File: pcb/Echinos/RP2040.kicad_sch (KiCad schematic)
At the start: 19 parts, among them U2 RP2040, X1 ASE-12MHz

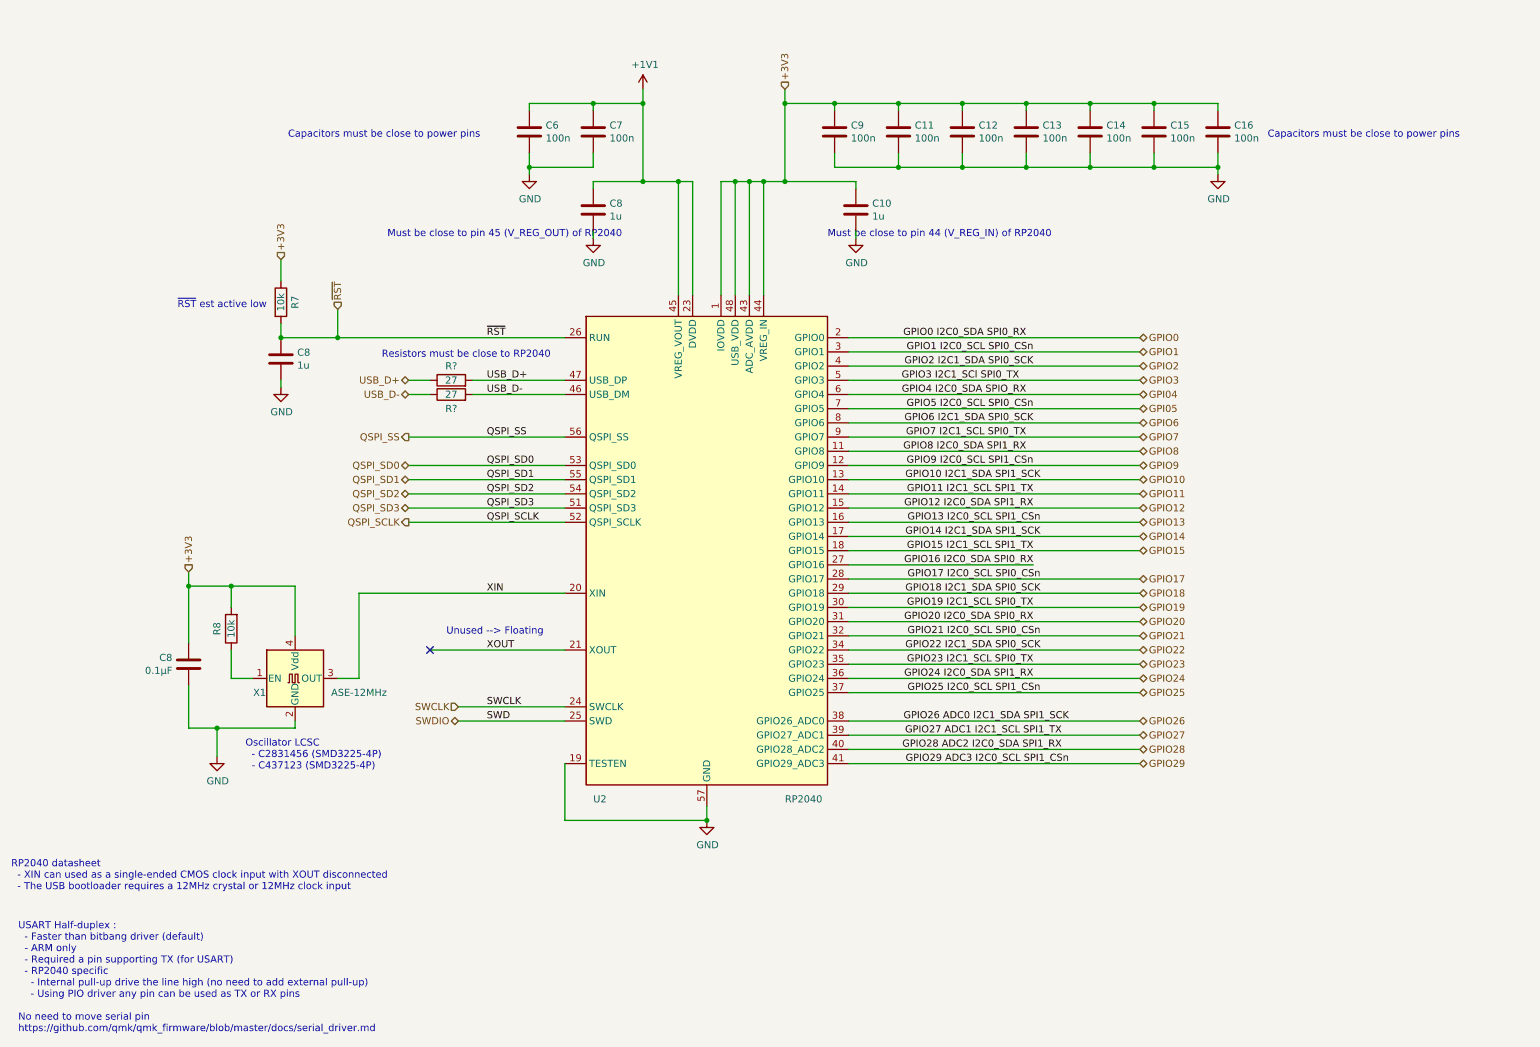
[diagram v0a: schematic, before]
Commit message: ✨ ♻️ 🚧 [PCB] - Continue draft schematic with:   - Keyboard matrix + Rotary encoder + analog joystick (specific sheet)   - Rename RP2040 sheet from untitled to RP2040 (make more sense ...)   - MCU first pin assignation
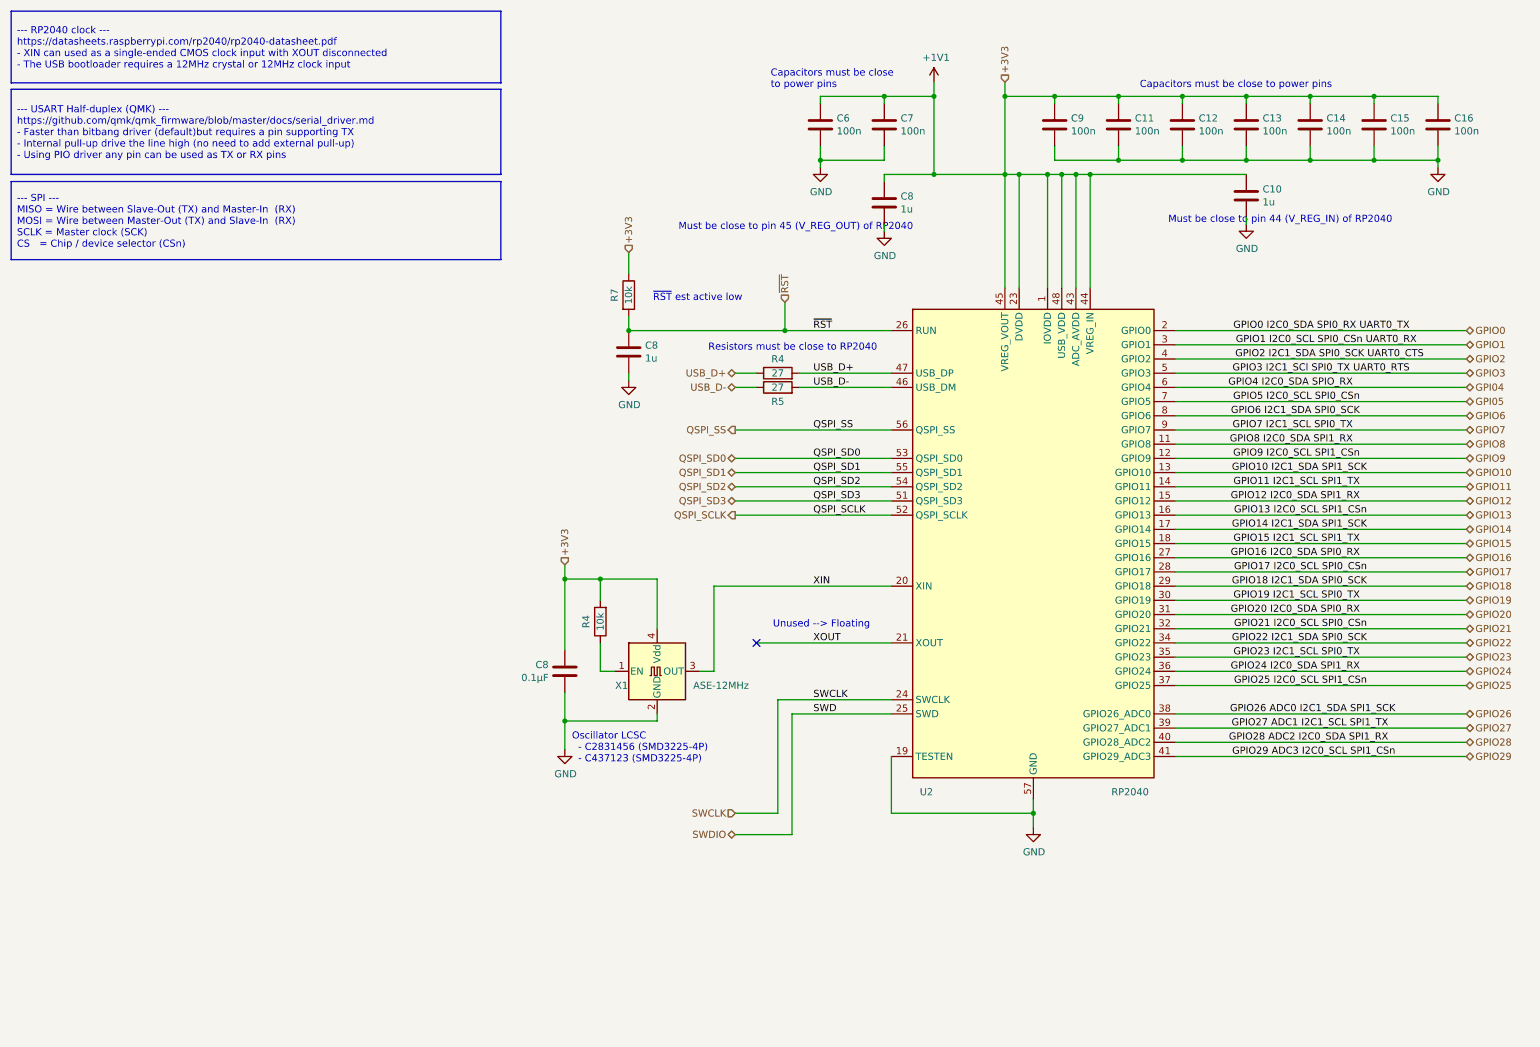
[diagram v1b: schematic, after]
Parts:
- gave numbers to parts that had none: 2
- renumbered R8 to R4
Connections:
- net +3V3 is gone; now on net +1V1: C10.1, C11.1, C12.1, C13.1, C14.1, C15.1, C16.1, C8.1, C9.1, R4.2, R7.1, U2.1 (IOVDD), U2.10 (IOVDD), U2.22 (IOVDD), U2.33 (IOVDD), U2.42 (IOVDD), U2.43 (ADC_AVDD), U2.44 (VREG_IN), U2.48 (USB_VDD), U2.49 (IOVDD), X1.4 (Vdd)
- net GPIO16 I2C0_SDA SPI0_RX renamed GPIO16
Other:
- note removed: "RP2040 datasheet - XIN can used as a single-ended CMOS clock input with XOUT disconnected - The USB bootloader requires a 12MHz crystal or 12MHz clock input"
- note removed: "USART Half-duplex : - Faster than bitbang driver (default) - ARM only - Required a pin supporting TX (for USART) - RP2040 specific - Internal pull-up drive the line high (no need to add external pull-up) - Using PIO driver any pin can be used as TX or RX pins No need to move serial pin https://github.com/qmk/qmk_firmware/blob/master/docs/serial_driver.md"
- moved on the sheet: C10, C11, C12, C13, C14, C15, C16, C6, C7, C8, C9, R4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

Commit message: ♻️ [PCB] - Remove symbol instances linking to other projets due to copy and paste of component symbol.
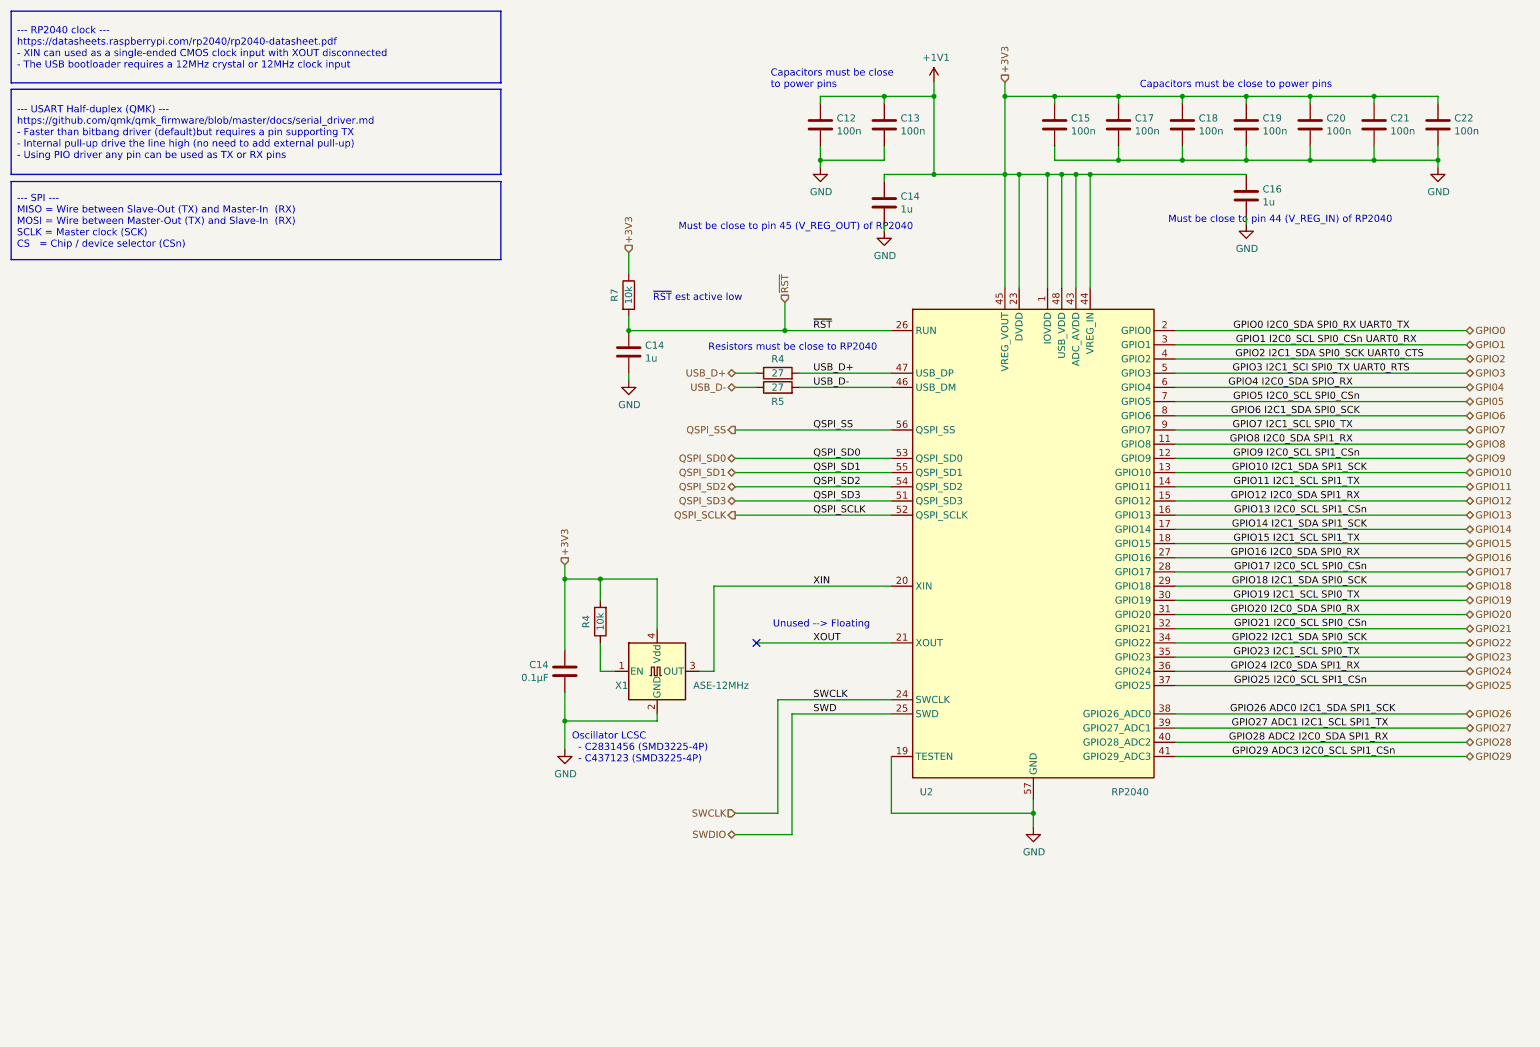
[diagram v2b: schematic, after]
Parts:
- renumbered C6 to C12, C7 to C13, C8 to C14, C9 to C15, C10 to C16, C11 to C17, C12 to C18, C13 to C19, C14 to C20, C15 to C21, C16 to C22

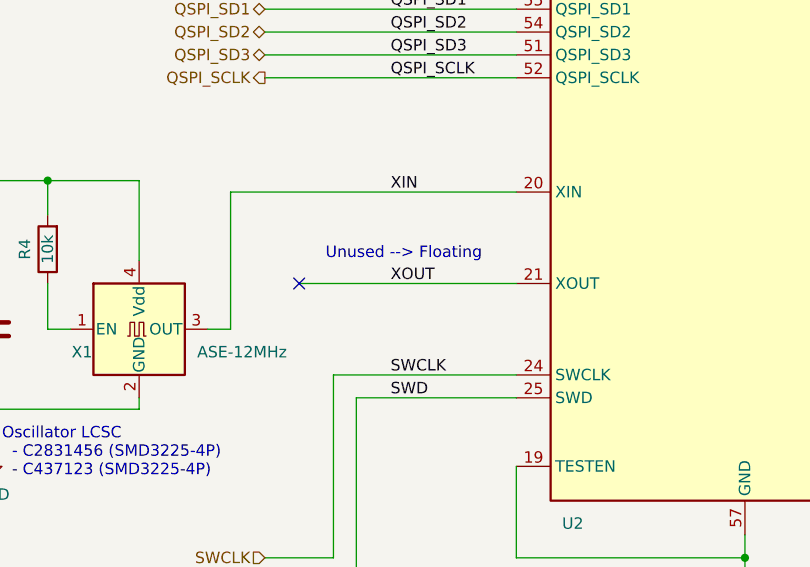
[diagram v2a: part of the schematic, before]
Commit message: ♻️ [PCB] - Add ferrite bead between shield and ground. Assign hand solder footprints whenever possible. Complete footprint assignation.
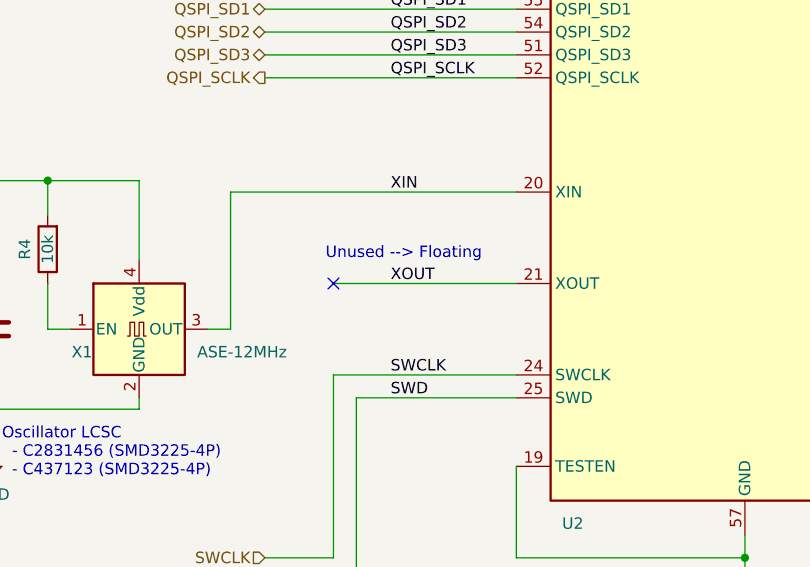
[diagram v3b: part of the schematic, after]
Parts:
- C12, C13, C14, C15, C16, C17, C18, C19, C20, C21, C22: footprint Capacitor_SMD:C_0402_1005Metric -> Capacitor_SMD:C_0402_1005Metric_Pad0.74x0.62mm_HandSolder
- R4, R5, R7: footprint Resistor_SMD:R_0402_1005Metric -> Resistor_SMD:R_0402_1005Metric_Pad0.72x0.64mm_HandSolder
- U2: footprint Package_DFN_QFN:QFN-56-1EP_7x7mm_P0.4mm_EP3.2x3.2mm -> Echinos:RP2040-QFN-56
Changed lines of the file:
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@@
   (junction (at 257.81 27.94) (diameter 0) (color 0 0 0 0)
   )
-  (no_connect (at 147.32 125.73))
+  (no_connect (at 151.13 125.73))
   (wire (pts (xy 204.47 41.91) (xy 201.93 41.91))
     (stroke (width 0) (type default))
@@
     (stroke (width 0) (type default))
   )
-  (wire (pts (xy 147.32 125.73) (xy 171.45 125.73))
+  (wire (pts (xy 151.13 125.73) (xy 171.45 125.73))
     (stroke (width 0) (type default))
   )
@@
       (effects (font (size 1.27 1.27)) (justify left))
     )
-    (property "Footprint" "Capacitor_SMD:C_0402_1005Metric" (at 235.9152 49.53 0)
+    (property "Footprint" "Capacitor_SMD:C_0402_1005Metric_Pad0.74x0.62mm_HandSolder" (at 235.9152 49.53 0)
       (effects (font (size 1.27 1.27)) hide)
     )
@@
       (effects (font (size 1.27 1.27)))
     )
-    (property "Footprint" "Resistor_SMD:R_0402_1005Metric" (at 122.682 63.5 90)
+    (property "Footprint" "Resistor_SMD:R_0402_1005Metric_Pad0.72x0.64mm_HandSolder" (at 122.682 63.5 90)
       (effects (font (size 1.27 1.27)) hide)
     )
@@
       (effects (font (size 1.27 1.27)) (justify left))
     )
-    (property "Footprint" "Capacitor_SMD:C_0402_1005Metric" (at 112.0648 134.62 0)
+    (property "Footprint" "Capacitor_SMD:C_0402_1005Metric_Pad0.74x0.62mm_HandSolder" (at 112.0648 134.62 0)
       (effects (font (size 1.27 1.27)) hide)
     )
@@
       (effects (font (size 1.27 1.27)) (justify left))
     )
-    (property "Footprint" "Capacitor_SMD:C_0402_1005Metric" (at 224.4852 36.83 0)
+    (property "Footprint" "Capacitor_SMD:C_0402_1005Metric_Pad0.74x0.62mm_HandSolder" (at 224.4852 36.83 0)
       (effects (font (size 1.27 1.27)) hide)
     )
@@
       (effects (font (size 1.27 1.27)) (justify left))
     )
-    (property "Footprint" "Capacitor_SMD:C_0402_1005Metric" (at 213.0552 36.83 0)
+    (property "Footprint" "Capacitor_SMD:C_0402_1005Metric_Pad0.74x0.62mm_HandSolder" (at 213.0552 36.83 0)
       (effects (font (size 1.27 1.27)) hide)
     )
@@
       (effects (font (size 1.27 1.27)) (justify left))
     )
-    (property "Footprint" "Capacitor_SMD:C_0402_1005Metric" (at 125.4252 77.47 0)
+    (property "Footprint" "Capacitor_SMD:C_0402_1005Metric_Pad0.74x0.62mm_HandSolder" (at 125.4252 77.47 0)
       (effects (font (size 1.27 1.27)) hide)
     )
@@
       (effects (font (size 1.27 1.27)) (justify left))
     )
-    (property "Footprint" "Capacitor_SMD:C_0402_1005Metric" (at 171.1452 36.83 0)
+    (property "Footprint" "Capacitor_SMD:C_0402_1005Metric_Pad0.74x0.62mm_HandSolder" (at 171.1452 36.83 0)
       (effects (font (size 1.27 1.27)) hide)
     )
@@
       (effects (font (size 1.27 1.27)) (justify left))
     )
-    (property "Footprint" "Capacitor_SMD:C_0402_1005Metric" (at 247.3452 36.83 0)
+    (property "Footprint" "Capacitor_SMD:C_0402_1005Metric_Pad0.74x0.62mm_HandSolder" (at 247.3452 36.83 0)
       (effects (font (size 1.27 1.27)) hide)
     )
@@
       (effects (font (size 1.27 1.27)) (justify left))
     )
-    (property "Footprint" "Capacitor_SMD:C_0402_1005Metric" (at 159.7152 36.83 0)
+    (property "Footprint" "Capacitor_SMD:C_0402_1005Metric_Pad0.74x0.62mm_HandSolder" (at 159.7152 36.83 0)
       (effects (font (size 1.27 1.27)) hide)
     )
@@
       (effects (font (size 1.27 1.27)) (justify left))
     )
-    (property "Footprint" "Capacitor_SMD:C_0402_1005Metric" (at 235.9152 36.83 0)
+    (property "Footprint" "Capacitor_SMD:C_0402_1005Metric_Pad0.74x0.62mm_HandSolder" (at 235.9152 36.83 0)
       (effects (font (size 1.27 1.27)) hide)
     )
@@
       (effects (font (size 1.27 1.27)) (justify left))
     )
-    (property "Footprint" "Capacitor_SMD:C_0402_1005Metric" (at 270.2052 36.83 0)
+    (property "Footprint" "Capacitor_SMD:C_0402_1005Metric_Pad0.74x0.62mm_HandSolder" (at 270.2052 36.83 0)
       (effects (font (size 1.27 1.27)) hide)
     )
@@
       (effects (font (size 1.27 1.27)))
     )
-    (property "Footprint" "Resistor_SMD:R_0402_1005Metric" (at 151.13 81.788 90)
+    (property "Footprint" "Resistor_SMD:R_0402_1005Metric_Pad0.72x0.64mm_HandSolder" (at 151.13 81.788 90)
       (effects (font (size 1.27 1.27)) hide)
     )
@@
       (effects (font (size 1.27 1.27)) (justify left))
     )
-    (property "Footprint" "Capacitor_SMD:C_0402_1005Metric" (at 171.1452 50.8 0)
+    (property "Footprint" "Capacitor_SMD:C_0402_1005Metric_Pad0.74x0.62mm_HandSolder" (at 171.1452 50.8 0)
       (effects (font (size 1.27 1.27)) hide)
     )
@@
       (effects (font (size 1.27 1.27)))
     )
-    (property "Footprint" "Resistor_SMD:R_0402_1005Metric" (at 121.158 121.92 90)
+    (property "Footprint" "Resistor_SMD:R_0402_1005Metric_Pad0.72x0.64mm_HandSolder" (at 121.158 121.92 90)
       (effects (font (size 1.27 1.27)) hide)
     )
@@
       (effects (font (size 1.27 1.27)) (justify left))
     )
-    (property "Footprint" "Capacitor_SMD:C_0402_1005Metric" (at 258.7752 36.83 0)
+    (property "Footprint" "Capacitor_SMD:C_0402_1005Metric_Pad0.74x0.62mm_HandSolder" (at 258.7752 36.83 0)
       (effects (font (size 1.27 1.27)) hide)
     )
@@
       (effects (font (size 1.27 1.27)) (justify left))
     )
-    (property "Footprint" "Package_DFN_QFN:QFN-56-1EP_7x7mm_P0.4mm_EP3.2x3.2mm" (at 196.85 107.95 0)
+    (property "Footprint" "Echinos:RP2040-QFN-56" (at 196.85 107.95 0)
       (effects (font (size 1.27 1.27)) hide)
     )
@@
       (effects (font (size 1.27 1.27)) (justify left))
     )
-    (property "Footprint" "Capacitor_SMD:C_0402_1005Metric" (at 201.6252 36.83 0)
+    (property "Footprint" "Capacitor_SMD:C_0402_1005Metric_Pad0.74x0.62mm_HandSolder" (at 201.6252 36.83 0)
       (effects (font (size 1.27 1.27)) hide)
     )
@@
       (effects (font (size 1.27 1.27)))
     )
-    (property "Footprint" "Resistor_SMD:R_0402_1005Metric" (at 151.13 79.248 90)
-      (effects (font (size 1.27 1.27)) hide)
-    )
+    (property "Footprint" "Resistor_SMD:R_0402_1005Metric_Pad0.72x0.64mm_HandSolder" (at 151.13 79.248 90)
+      (effects (font (size 1.27 1.27)) hide)
+    )
